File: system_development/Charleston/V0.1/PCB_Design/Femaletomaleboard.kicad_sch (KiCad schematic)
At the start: 5 parts, among them J1 DB25_Receptacle, J2 Screw_Terminal_01x12, J3 Screw_Terminal_01x12

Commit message: femaletomaleboard
4th times the charm
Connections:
- net at J1.5: no longer J2.10 (Pin_10)
- now unconnected: J1.1, J2.1 (Pin_1), U1.1

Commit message: updates
updates
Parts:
- J1: symbol Connector:DB25_Receptacle -> libary_bms:DB25_Receptacle
- J2, J3: symbol Connector:Screw_Terminal_01x12 -> libary_bms:Screw_Terminal_01x12
- U1, U2: symbol Gold_Finger_connector:GoldFingerConnector -> libary_bms:GoldFingerConnector
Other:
- moved on the sheet: U2
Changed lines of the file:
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@@
 (kicad_sch (version 20230121) (generator eeschema)
   (paper "A4")
-  (symbol (lib_id "Connector:Screw_Terminal_01x12") (at 93.7895 114.7445 270) (unit 1)
+  (symbol (lib_id "libary_bms:Screw_Terminal_01x12") (at 93.7895 114.7445 270) (unit 1)
     (in_bom yes) (on_board yes) (dnp no) (fields_autoplaced)
     (property "Reference" "J3" (at 92.5195 118.1735 90)
@@
     )
   )
-  (symbol (lib_id "Gold_Finger_connector:GoldFingerConnector") (at 74.549 66.548 180) (unit 1)
+  (symbol (lib_id "libary_bms:GoldFingerConnector") (at 74.549 69.215 180) (unit 1)
     (in_bom yes) (on_board yes) (dnp no)
-    (property "Reference" "U2" (at 69.088 54.677 0)
+    (property "Reference" "U2" (at 69.088 57.344 0)
       (effects (font (size 1.27 1.27)))
     )
-    (property "Value" "~" (at 74.549 66.548 0)
+    (property "Value" "~" (at 74.549 69.215 0)
       (effects (font (size 1.27 1.27)))
     )
-    (property "Footprint" "" (at 74.549 66.548 0)
+    (property "Footprint" "" (at 74.549 69.215 0)
       (effects (font (size 1.27 1.27)) hide)
     )
-    (property "Datasheet" "" (at 74.549 66.548 0)
+    (property "Datasheet" "" (at 74.549 69.215 0)
       (effects (font (size 1.27 1.27)) hide)
     )
@@
     )
   )
-  (symbol (lib_id "Connector:DB25_Receptacle") (at 122.301 61.849 0) (unit 1)
+  (symbol (lib_id "libary_bms:DB25_Receptacle") (at 122.301 61.849 0) (unit 1)
     (in_bom yes) (on_board yes) (dnp no)
     (property "Reference" "J1" (at 109.1565 118.5545 0)
@@
     )
   )
-  (symbol (lib_id "Gold_Finger_connector:GoldFingerConnector") (at 74.549 22.673 180) (unit 1)
+  (symbol (lib_id "libary_bms:GoldFingerConnector") (at 74.549 22.673 180) (unit 1)
     (in_bom yes) (on_board yes) (dnp no)
     (property "Reference" "U1" (at 68.834 19.244 0)
@@
     )
   )
-  (symbol (lib_id "Connector:Screw_Terminal_01x12") (at 98.044 16.51 90) (unit 1)
+  (symbol (lib_id "libary_bms:Screw_Terminal_01x12") (at 98.044 16.51 90) (unit 1)
     (in_bom yes) (on_board yes) (dnp no) (fields_autoplaced)
     (property "Reference" "J2" (at 99.314 10.16 90)

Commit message: Assembled Libraries
Assembled Libraries
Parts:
- added U1: ~, infnoise_goldfingers:Gold Finger single, symbol libary_bms:Goldfingersingle
- J1: renamed from J3; footprint (none) -> infnoise_goldfingers:Gold Finger single
- J2: footprint (none) -> TerminalBlock_Altech:Altech_AK300_1x12_P5.00mm_45-Degree
- U2: renamed from U1; footprint (none) -> infnoise_goldfingers:Gold Finger PCB
- U3: renamed from U2; footprint (none) -> infnoise_goldfingers:Gold Finger PCB
- renumbered J1 to J3
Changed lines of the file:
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@@
   (symbol (lib_id "libary_bms:Screw_Terminal_01x12") (at 93.7895 114.7445 270) (unit 1)
     (in_bom yes) (on_board yes) (dnp no) (fields_autoplaced)
-    (property "Reference" "J3" (at 92.5195 118.1735 90)
+    (property "Reference" "J1" (at 92.5195 118.1735 90)
       (effects (font (size 1.27 1.27)))
     )
@@
       (effects (font (size 1.27 1.27)))
     )
-    (property "Footprint" "" (at 93.7895 114.7445 0)
+    (property "Footprint" "infnoise_goldfingers:Gold Finger single" (at 93.7895 114.7445 0)
       (effects (font (size 1.27 1.27)) hide)
     )
@@
       (project "Femaletomaleboard"
         (path "/8dcdbe00-6c4e-43b9-b640-476052a1e30f"
-          (reference "J3") (unit 1)
+          (reference "J1") (unit 1)
         )
       )
@@
   (symbol (lib_id "libary_bms:GoldFingerConnector") (at 74.549 69.215 180) (unit 1)
     (in_bom yes) (on_board yes) (dnp no)
-    (property "Reference" "U2" (at 69.088 57.344 0)
+    (property "Reference" "U3" (at 69.088 57.344 0)
       (effects (font (size 1.27 1.27)))
     )
@@
       (effects (font (size 1.27 1.27)))
     )
-    (property "Footprint" "" (at 74.549 69.215 0)
+    (property "Footprint" "infnoise_goldfingers:Gold Finger PCB" (at 74.549 69.215 0)
       (effects (font (size 1.27 1.27)) hide)
     )
@@
       (project "Femaletomaleboard"
         (path "/8dcdbe00-6c4e-43b9-b640-476052a1e30f"
-          (reference "U2") (unit 1)
+          (reference "U3") (unit 1)
+        )
+      )
+    )
+  )
+  (symbol (lib_id "libary_bms:Goldfingersingle") (at 16.383 53.721 0) (unit 1)
+    (in_bom yes) (on_board yes) (dnp no) (fields_autoplaced)
+    (property "Reference" "U1" (at 20.193 54.356 0)
+      (effects (font (size 1.27 1.27)) (justify left) hide)
+    )
+    (property "Value" "~" (at 16.383 53.721 0)
+      (effects (font (size 1.27 1.27)))
+    )
+    (property "Footprint" "infnoise_goldfingers:Gold Finger single" (at 16.383 53.721 0)
+      (effects (font (size 1.27 1.27)) hide)
+    )
+    (property "Datasheet" "" (at 16.383 53.721 0)
+      (effects (font (size 1.27 1.27)) hide)
+    )
+    (instances
+      (project "Femaletomaleboard"
+        (path "/8dcdbe00-6c4e-43b9-b640-476052a1e30f"
+          (reference "U1") (unit 1)
         )
       )
@@
   (symbol (lib_id "libary_bms:DB25_Receptacle") (at 122.301 61.849 0) (unit 1)
     (in_bom yes) (on_board yes) (dnp no)
-    (property "Reference" "J1" (at 109.1565 118.5545 0)
+    (property "Reference" "J3" (at 109.1565 118.5545 0)
       (effects (font (size 1.27 1.27)) (justify left))
     )
@@
       (project "Femaletomaleboard"
         (path "/8dcdbe00-6c4e-43b9-b640-476052a1e30f"
-          (reference "J1") (unit 1)
+          (reference "J3") (unit 1)
         )
       )
@@
   (symbol (lib_id "libary_bms:GoldFingerConnector") (at 74.549 22.673 180) (unit 1)
     (in_bom yes) (on_board yes) (dnp no)
-    (property "Reference" "U1" (at 68.834 19.244 0)
+    (property "Reference" "U2" (at 68.834 19.244 0)
       (effects (font (size 1.27 1.27)))
     )
@@
       (effects (font (size 1.27 1.27)))
     )
-    (property "Footprint" "" (at 74.549 22.673 0)
+    (property "Footprint" "infnoise_goldfingers:Gold Finger PCB" (at 74.549 22.673 0)
       (effects (font (size 1.27 1.27)) hide)
     )
@@
       (project "Femaletomaleboard"
         (path "/8dcdbe00-6c4e-43b9-b640-476052a1e30f"
-          (reference "U1") (unit 1)
+          (reference "U2") (unit 1)
         )
       )
@@
       (effects (font (size 1.27 1.27)))
     )
-    (property "Footprint" "" (at 98.044 16.51 0)
+    (property "Footprint" "TerminalBlock_Altech:Altech_AK300_1x12_P5.00mm_45-Degree" (at 98.044 16.51 0)
       (effects (font (size 1.27 1.27)) hide)
     )

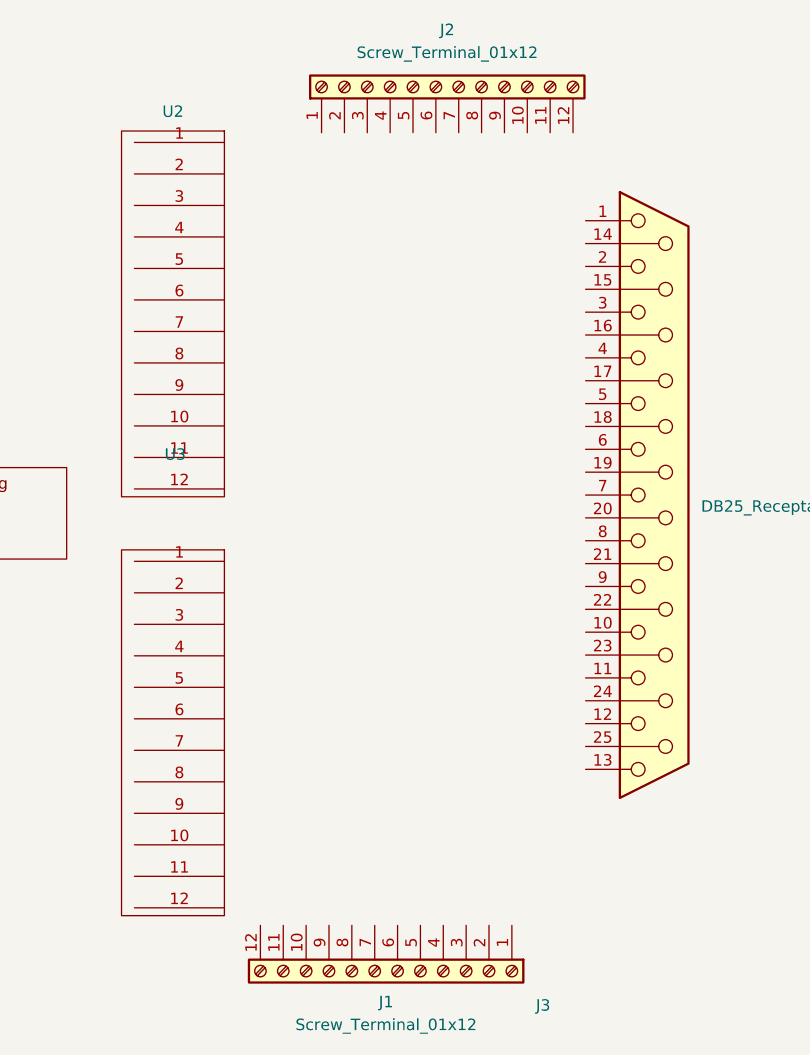
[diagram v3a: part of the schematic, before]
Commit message: Added wires no Errors
Added wires, no errors just grid warnings. The 2 errors left should be completely fine.
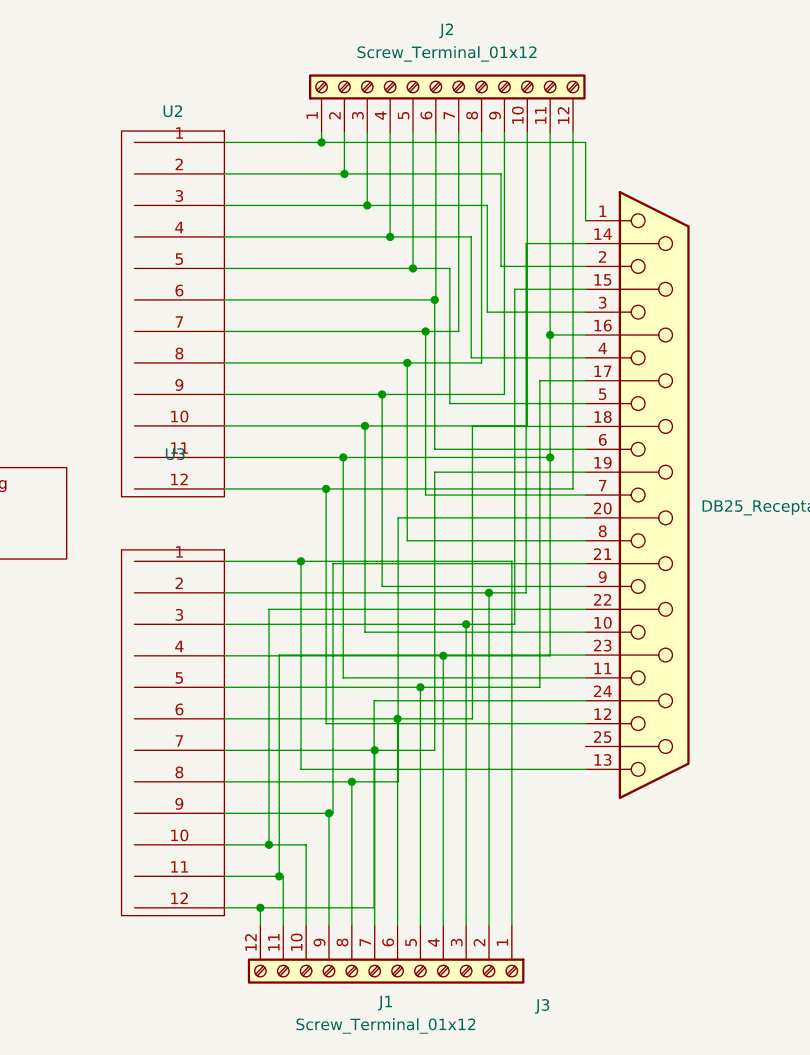
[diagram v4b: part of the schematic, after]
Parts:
- U?: renamed from U1; footprint infnoise_goldfingers:Gold Finger single -> (none)
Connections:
- net at J1.1 (Pin_1): now also J3.13, U3.1
- net at J1.10 (Pin_10): now also J3.22 (P22), U3.10
- net at J1.11 (Pin_11): now also J3.23 (P23), U3.11
- net at J1.12 (Pin_12): now also J3.24 (P24), U3.12
- net at J1.2 (Pin_2): now also J3.14 (P14), U3.2
- net at J1.3 (Pin_3): now also J3.15 (P15), U3.3
- net at J1.4 (Pin_4): now also J2.11 (Pin_11), J3.11, J3.16 (P16), U2.11, U3.4
- net at J1.5 (Pin_5): now also J3.17 (P17), U3.5
- net at J1.6 (Pin_6): now also J3.18 (P18), U3.6
- net at J1.7 (Pin_7): now also J3.19 (P19), U3.7
- net at J1.8 (Pin_8): now also J3.20 (P20), U3.8
- net at J1.9 (Pin_9): now also J3.21 (P21), U3.9
- net at J3.1: now also J2.1 (Pin_1), U2.1
- net at J3.10: now also J2.10 (Pin_10), U2.10
- net at J3.12: now also J2.12 (Pin_12), U2.12
- net at J3.2: now also J2.2 (Pin_2), U2.2
- net at J3.3: now also J2.3 (Pin_3), U2.3
- net at J3.4: now also J2.4 (Pin_4), U2.4
- net at J3.5: now also J2.5 (Pin_5), U2.5
- net at J3.6: now also J2.6 (Pin_6), U2.6
- net at J3.7: now also J2.7 (Pin_7), U2.7
- net at J3.8: now also J2.8 (Pin_8), U2.8
- net at J3.9: now also J2.9 (Pin_9), U2.9

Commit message: did it correctly with netlist and all.
Re did it with same desgin but with netlist and proper way
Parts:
- removed J1: Screw_Terminal_01x12, infnoise_goldfingers:Gold Finger single, symbol libary_bms:Screw_Terminal_01x12
- removed U?: ~, symbol libary_bms:Goldfingersingle
- added J4: Screw_Terminal_01x12, TerminalBlock_Altech:Altech_AK300_1x12_P5.00mm_45-Degree, symbol screw_terminal_01x12:Screw_Terminal_01x12
- J3: footprint Connector_Dsub:DSUB-25_Male_Horizontal_P2.77x2.54mm_EdgePinOffset9.40mm -> Connector_Dsub:DSUB-25_Female_Horizontal_P2.77x2.54mm_EdgePinOffset9.40mm
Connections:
- net at J3.13, U3.1: now also J4.12 (Pin_12)
- net at J3.22 (P22), U3.10: now also J4.3 (Pin_3)
- net at J3.23 (P23), U3.11: now also J4.2 (Pin_2)
- net at J3.24 (P24), U3.12: now also J4.1 (Pin_1)
- net at J3.14 (P14), U3.2: now also J4.11 (Pin_11)
- net at J3.15 (P15), U3.3: now also J4.10 (Pin_10)
- net at J3.11, J3.16 (P16), U2.11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: now also J2.2 (Pin_2), J4.9 (Pin_9); no longer J2.11 (Pin_11)
- net at J3.17 (P17), U3.5: now also J4.8 (Pin_8)
- net at J3.18 (P18), U3.6: now also J4.7 (Pin_7)
- net at J3.19 (P19), U3.7: now also J4.6 (Pin_6)
- net at J3.20 (P20), U3.8: now also J4.5 (Pin_5)
- net at J3.21 (P21), U3.9: now also J4.4 (Pin_4)
- net at J3.1, U2.1: now also J2.12 (Pin_12); no longer J2.1 (Pin_1)
- net at J3.10, U2.10: now also J2.3 (Pin_3); no longer J2.10 (Pin_10)
- net at J3.12, U2.12: now also J2.1 (Pin_1); no longer J2.12 (Pin_12)
- net at J3.2, U2.2: now also J2.11 (Pin_11); no longer J2.2 (Pin_2)
- net unconnected-(J3-P25-Pad25): now reaches J3.25 (P25)
- net at J3.3, U2.3: now also J2.10 (Pin_10); no longer J2.3 (Pin_3)
- net at J3.4, U2.4: now also J2.9 (Pin_9); no longer J2.4 (Pin_4)
- net at J3.5, U2.5: now also J2.8 (Pin_8); no longer J2.5 (Pin_5)
- net at J3.6, U2.6: now also J2.7 (Pin_7); no longer J2.6 (Pin_6)
- net at J3.7, U2.7: now also J2.6 (Pin_6); no longer J2.7 (Pin_7)
- net at J3.8, U2.8: now also J2.5 (Pin_5); no longer J2.8 (Pin_8)
- net at J3.9, U2.9: now also J2.4 (Pin_4); no longer J2.9 (Pin_9)
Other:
- moved on the sheet: J2, U2, U3
